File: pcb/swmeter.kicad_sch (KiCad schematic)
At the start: 23 parts, among them J0 Conn_01x02_Female, J1 AudioPlug, J2 Conn_Coaxial, J3 Conn_01x03_Female, SW1 SW_SPDT, SW2 SW_SPDT, SW3 SW_DIP_x02, U1 LM3914N

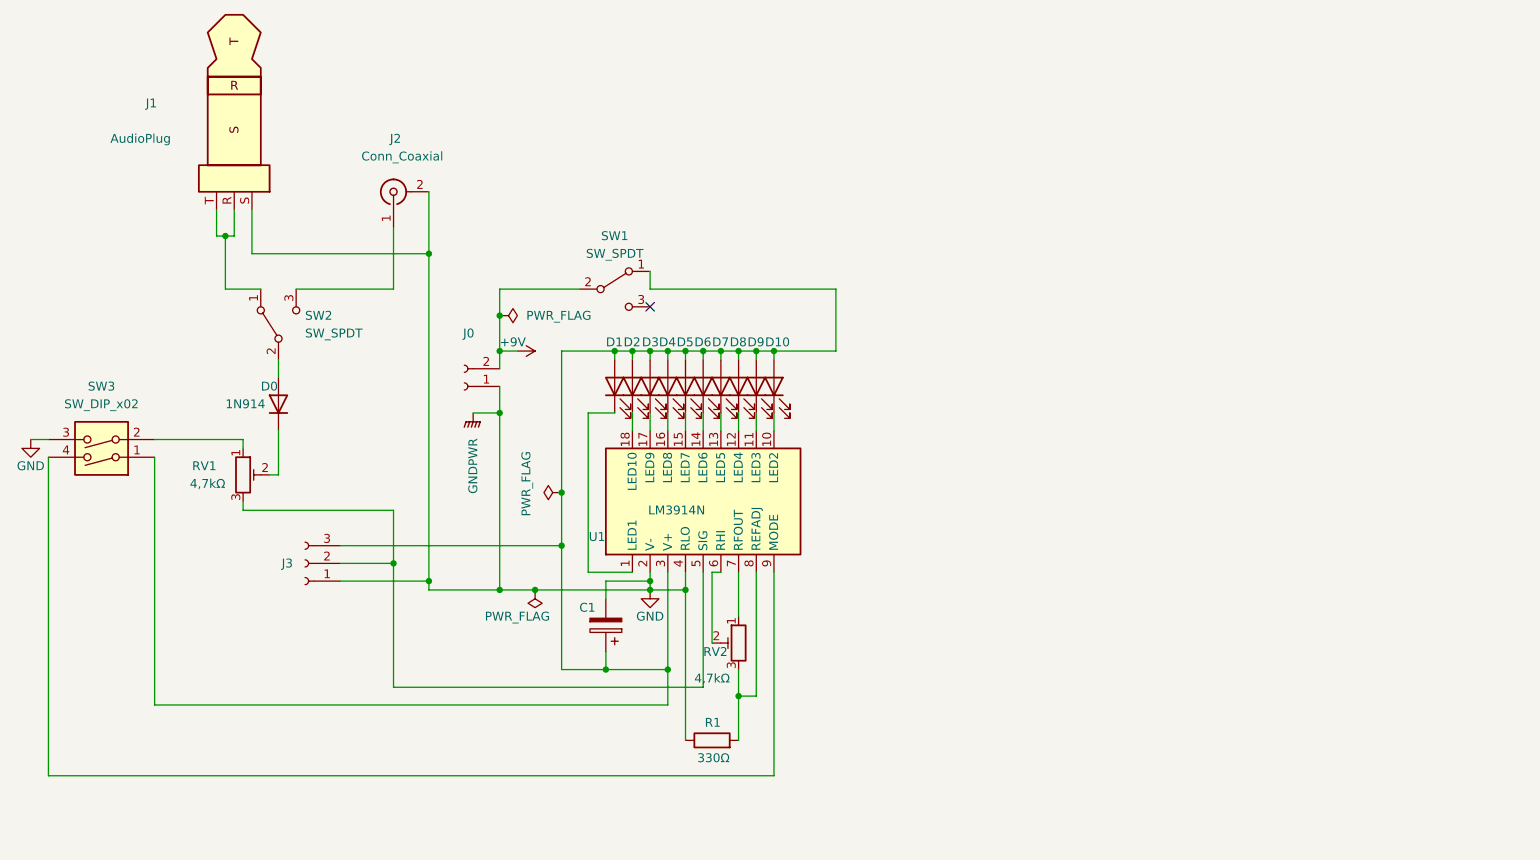
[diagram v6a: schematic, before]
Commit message: -update to compact bargraph design -add capacitor for battery
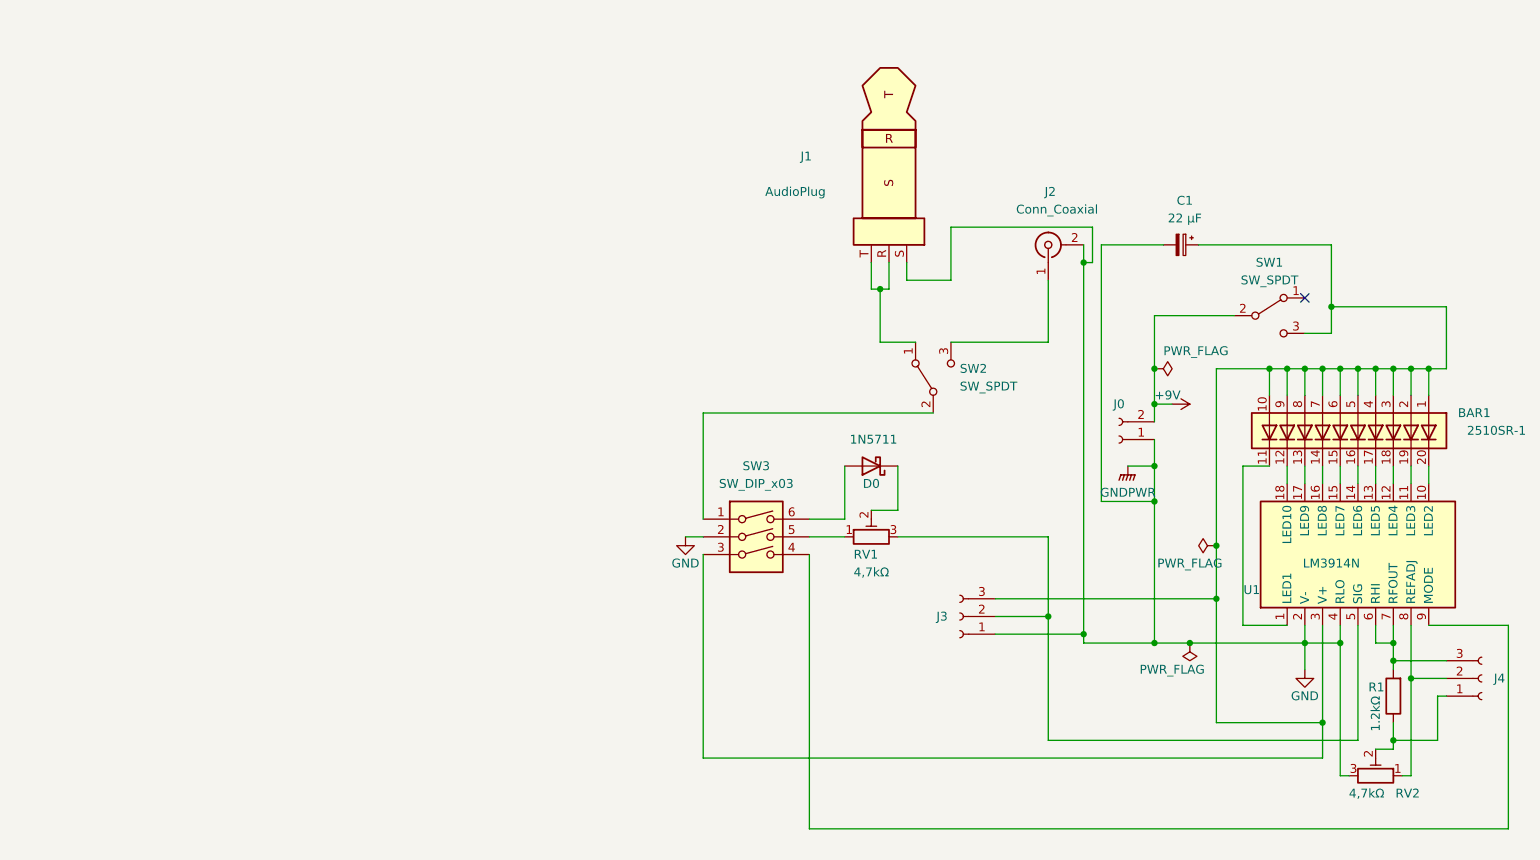
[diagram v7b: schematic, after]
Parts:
- removed C1: (no value), Capacitor_THT:CP_Radial_D5.0mm_P2.50mm, symbol Device:C_Polarized
- removed D0: 1N914, Diode_THT:D_DO-35_SOD27_P7.62mm_Horizontal, symbol Diode:1N914
- removed D1, D10, D3, D4, D5, D6, D7, D8, D9: LED, LED_THT:LED_D3.0mm_Clear, symbol Device:LED
- removed D2: red, LED_THT:LED_D3.0mm_Clear, symbol Device:LED
- removed SW3: SW_DIP_x02, Button_Switch_THT:SW_DIP_SPSTx02_Slide_6.7x6.64mm_W7.62mm_P2.54mm_LowProfile, symbol Switch:SW_DIP_x02
- added BAR1: 2510SR-1, Display:HDSP-4836, symbol LED:HDSP-4836_2
- added C1: 22 µF, Capacitor_THT:CP_Radial_D4.0mm_P2.00mm, symbol Device:C_Polarized_Small
- added D0: 1N5711, Diode_THT:D_DO-35_SOD27_P7.62mm_Horizontal, symbol Diode:1N5711
- added J4: Conn_01x03_Female, Connector_PinHeader_1.27mm:PinHeader_1x03_P1.27mm_Vertical, symbol Connector:Conn_01x03_Female
- added SW3: SW_DIP_x03, Button_Switch_THT:SW_DIP_SPSTx03_Slide_9.78x9.8mm_W7.62mm_P2.54mm, symbol Switch:SW_DIP_x03
- R1: value 330Ω -> 1.2kΩ
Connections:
- net GND: now also RV2.3, C1.2, SW3.2; no longer R1.1
- net at J3.3 (Pin_3), U1.3 (V+): now also SW1.3 (C), BAR1.1 (A), BAR1.10 (A), BAR1.2 (A), BAR1.3 (A), BAR1.4 (A), BAR1.5 (A), BAR1.6 (A), BAR1.7 (A), BAR1.8 (A), BAR1.9 (A), C1.1, SW3.3; no longer SW1.1 (A)
- net at U1.1 (LED1): now also BAR1.11 (K)
- net at SW2.2 (B): now also SW3.1
- net at RV1.1: now also SW3.5
- net at RV1.2: now also D0.1 (K)
- net at U1.18 (LED10): now also BAR1.12 (K)
- net at U1.13 (LED5): now also BAR1.17 (K)
- net at U1.16 (LED8): now also BAR1.14 (K)
- net at U1.10 (LED2): now also BAR1.20 (K)
- net at U1.11 (LED3): now also BAR1.19 (K)
- net at U1.12 (LED4): now also BAR1.18 (K)
- net at U1.14 (LED6): now also BAR1.16 (K)
- net at U1.15 (LED7): now also BAR1.15 (K)
- net at U1.17 (LED9): now also BAR1.13 (K)
- net at RV2.2: now also R1.1, J4.1 (Pin_1); no longer U1.6 (RHI)
- net at U1.7 (RFOUT): now also R1.2, U1.6 (RHI), J4.3 (Pin_3); no longer RV2.1
- net at U1.9 (MODE): now also SW3.4
- new net: D0.2 (A), SW3.6
- new net: J4.2 (Pin_2), RV2.1, U1.8 (REFADJ)
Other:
- moved on the sheet: J0, J1, J2, J3, RV1, SW1, SW2, U1

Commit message: optimized trimmer schematics
optimized trimmer schematics
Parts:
- added RV3: 1,2kΩ, Potentiometer_THT:Potentiometer_Bourns_3266Y_Vertical, symbol Device:R_Potentiometer_Trim
- J3, J4: footprint Connector_PinHeader_1.27mm:PinHeader_1x03_P1.27mm_Vertical -> Connector_PinHeader_2.54mm:PinHeader_1x03_P2.54mm_Vertical
- R1: value 1.2kΩ -> R; footprint Resistor_THT:R_Axial_DIN0207_L6.3mm_D2.5mm_P10.16mm_Horizontal -> Resistor_THT:R_Axial_DIN0207_L6.3mm_D2.5mm_P7.62mm_Horizontal
- SW1: footprint Button_Switch_THT:SW_E-Switch_EG1224_SPDT_Angled -> Button_Switch_THT:SW_Slide_1P2T_CK_OS102011MS2Q
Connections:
- net GND: now also J4.1 (Pin_1), RV2.2
- net at BAR1.1 (A), BAR1.10 (A), BAR1.2 (A)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: now also R1.2; no longer C1.1, J3.3 (Pin_3), SW1.3 (C), SW3.3, U1.3 (V+)
- net at J4.3 (Pin_3), U1.6 (RHI), U1.7 (RFOUT): now also RV3.1, RV3.2; no longer R1.2
- net at J4.2 (Pin_2), RV2.1, U1.8 (REFADJ): now also RV3.3
- new net: C1.1, J3.3 (Pin_3), R1.1, SW1.3 (C), SW3.3, U1.3 (V+)
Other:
- moved on the sheet: J4
